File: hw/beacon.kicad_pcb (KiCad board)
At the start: 2 copper layers, 36 x 36 mm, 22 parts, among them J1 SPI_Prog_conn, Q1 Q_NMOS_DGS, Q2 Q_NMOS_DGS, Q3 Q_NMOS_DGS, U1 ATmega328-AU, U2 TSOP382xx

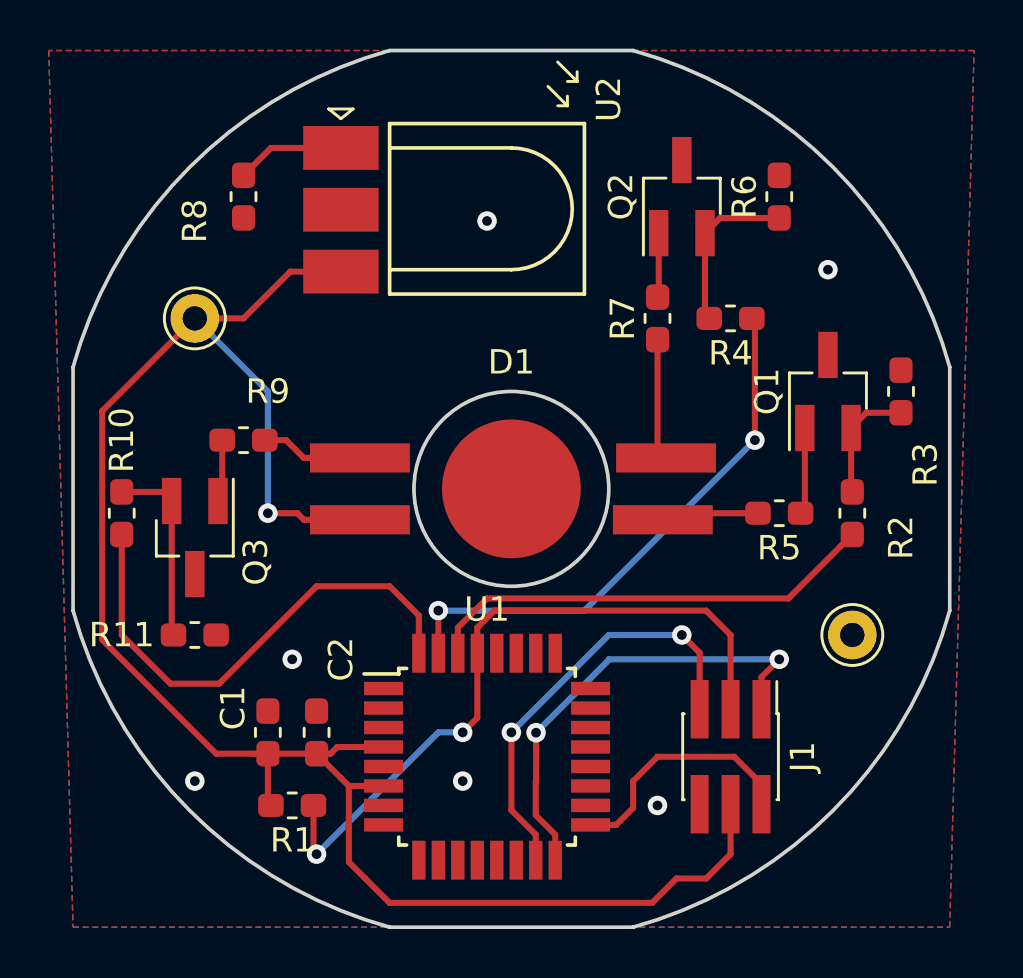
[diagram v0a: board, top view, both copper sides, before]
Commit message: Fixed hardware design errors
Missing connection between IR sensor and MCU
Wrong footprint for transistors
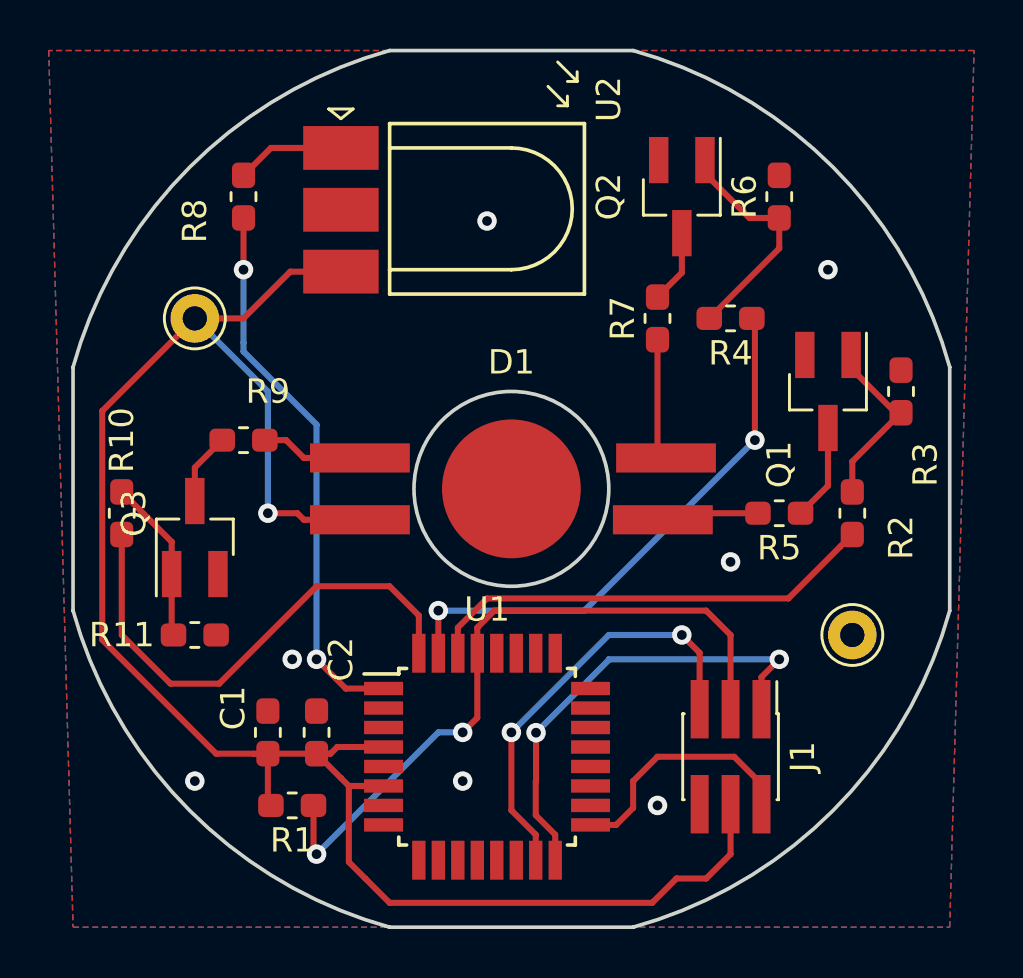
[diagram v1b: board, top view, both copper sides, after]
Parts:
- Q1, Q2, Q3: value Q_NMOS_DGS -> Q_NMOS_GSD
- turned Q1 to 270 degrees
- turned Q2 to 270 degrees
- turned Q3 to 90 degrees
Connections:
- Q1 pad 2: Net-(Q1-Pad2) -> GND
- Q1 pad 3: GND -> Net-(Q1-Pad3)
- Q2 pad 2: Net-(Q2-Pad2) -> GND
- Q2 pad 3: GND -> Net-(Q2-Pad3)
- Q3 pad 2: Net-(Q3-Pad2) -> GND
- Q3 pad 3: GND -> Net-(Q3-Pad3)
- R10 pad 2: Net-(Q3-Pad2) -> Net-(Q3-Pad1)
- R11 pad 1: Net-(Q3-Pad2) -> Net-(Q3-Pad1)
- R2 pad 2: Net-(Q1-Pad2) -> Net-(Q1-Pad1)
- R3 pad 1: Net-(Q1-Pad2) -> Net-(Q1-Pad1)
- R4 pad 2: Net-(Q2-Pad2) -> Net-(Q2-Pad1)
- R5 pad 1: Net-(Q1-Pad1) -> Net-(Q1-Pad3)
- R6 pad 1: Net-(Q2-Pad2) -> Net-(Q2-Pad1)
- R7 pad 2: Net-(Q2-Pad1) -> Net-(Q2-Pad3)
- R9 pad 2: Net-(Q3-Pad1) -> Net-(Q3-Pad3)
- U1 pad 1: Net-(U1-Pad1) -> /IR_MCU_IN
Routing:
- net /IR_MCU_IN: track 0.00 -> 22.6 mm, vias 0 -> 2
- net Net-(Q3-Pad2): track 7.74 -> 0.00 mm
- net Net-(Q2-Pad1): track 2.65 -> 9.67 mm
- net Net-(Q2-Pad2): track 6.88 -> 0.00 mm
- net Net-(Q1-Pad2): track 4.95 -> 0.00 mm
- net Net-(Q3-Pad1): track 2.57 -> 6.76 mm
- net Net-(Q1-Pad3): track 0.00 -> 3.97 mm
- net Net-(Q1-Pad1): track 3.57 -> 7.43 mm
- net Net-(Q2-Pad3): track 0.00 -> 3.04 mm
- net Net-(Q3-Pad3): track 0.00 -> 2.97 mm
- net GND: vias 6 -> 7
